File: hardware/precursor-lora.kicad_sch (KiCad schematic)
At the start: 12 parts, among them J1 PRECURSOR_CONN, J2 U.FL, U1 RAK3172, U2 AP2112K-3.3

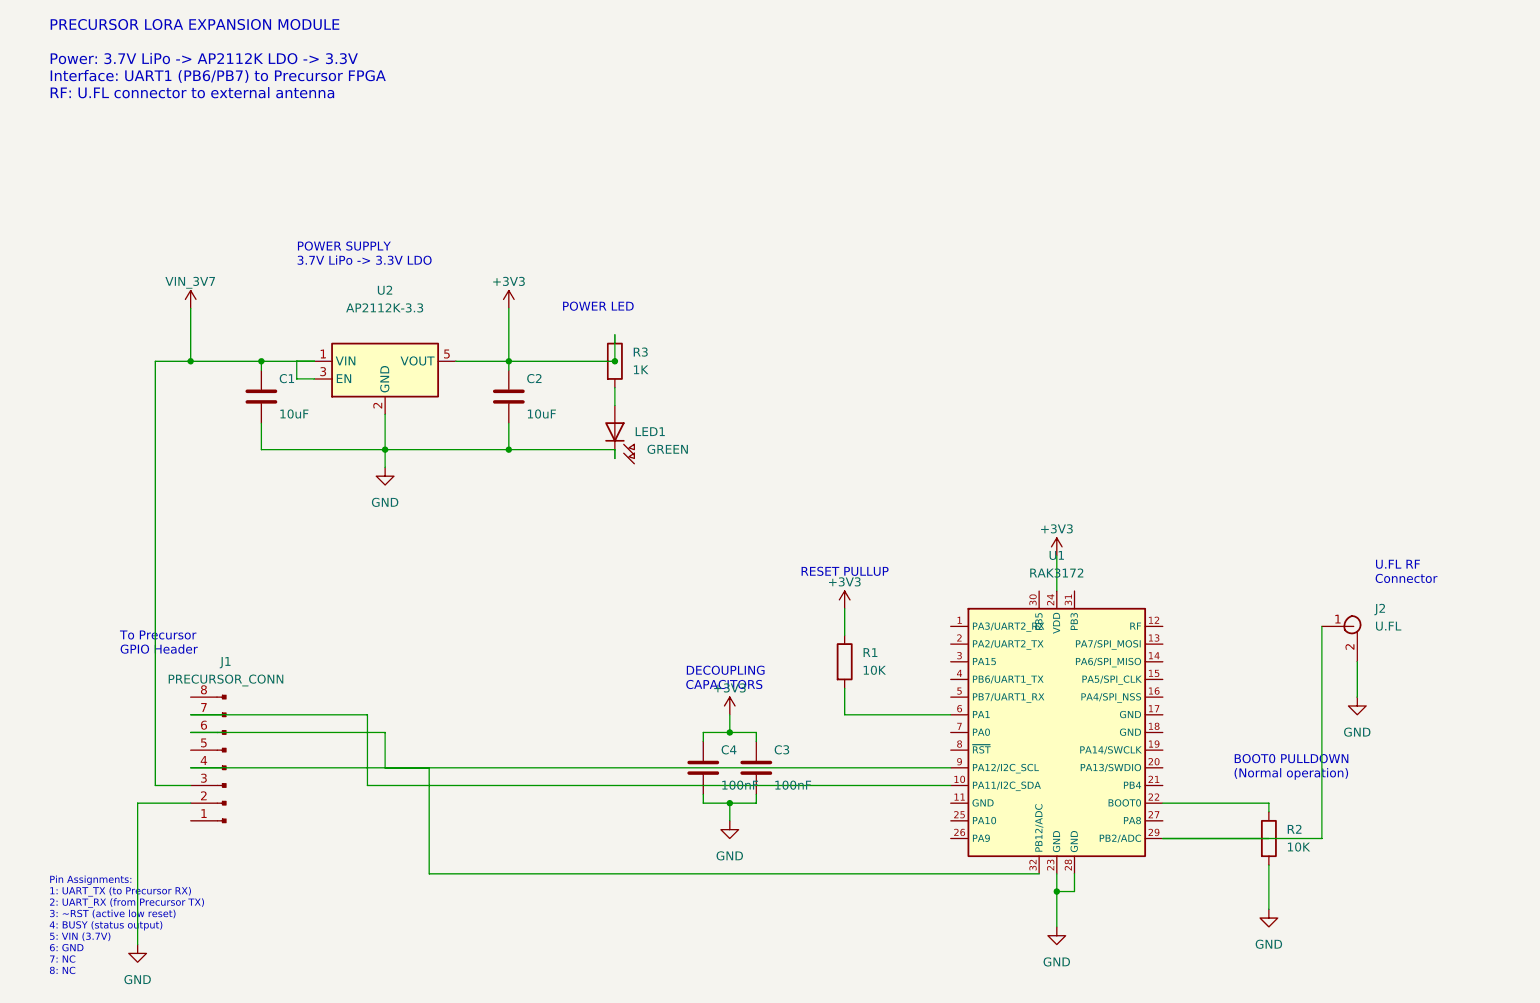
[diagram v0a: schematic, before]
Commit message: Fix RAK3172 pinout and schematic wiring - verified against datasheet
- Corrected RAK3172 symbol pinout to match official datasheet:
  * Pin 4: PB6/UART1_TX
  * Pin 5: PB7/UART1_RX
  * Pin 12: RF
  * Pin 21: BOOT0
  * Pin 22: RST (active low)
  * Pin 24: VDD
  * GND: pins 11, 17, 18, 23, 28
- Fixed BOOT0 pulldown circuit (was incorrectly connected to RST network)
- Fixed RST pullup circuit wiring
- All signal connections verified:
  * J1.1 -> UART1_TX (PB6)
  * J1.2 -> UART1_RX (PB7)
  * J1.3 -> RST with 10K pullup
  * J1.4 -> PB5 (BUSY status)
  * J1.5 -> VIN (3.7V)
  * J1.6 -> GND
- Rev 1.2

Co-Authored-By: Claude Opus 4.5 <noreply@anthropic.com>
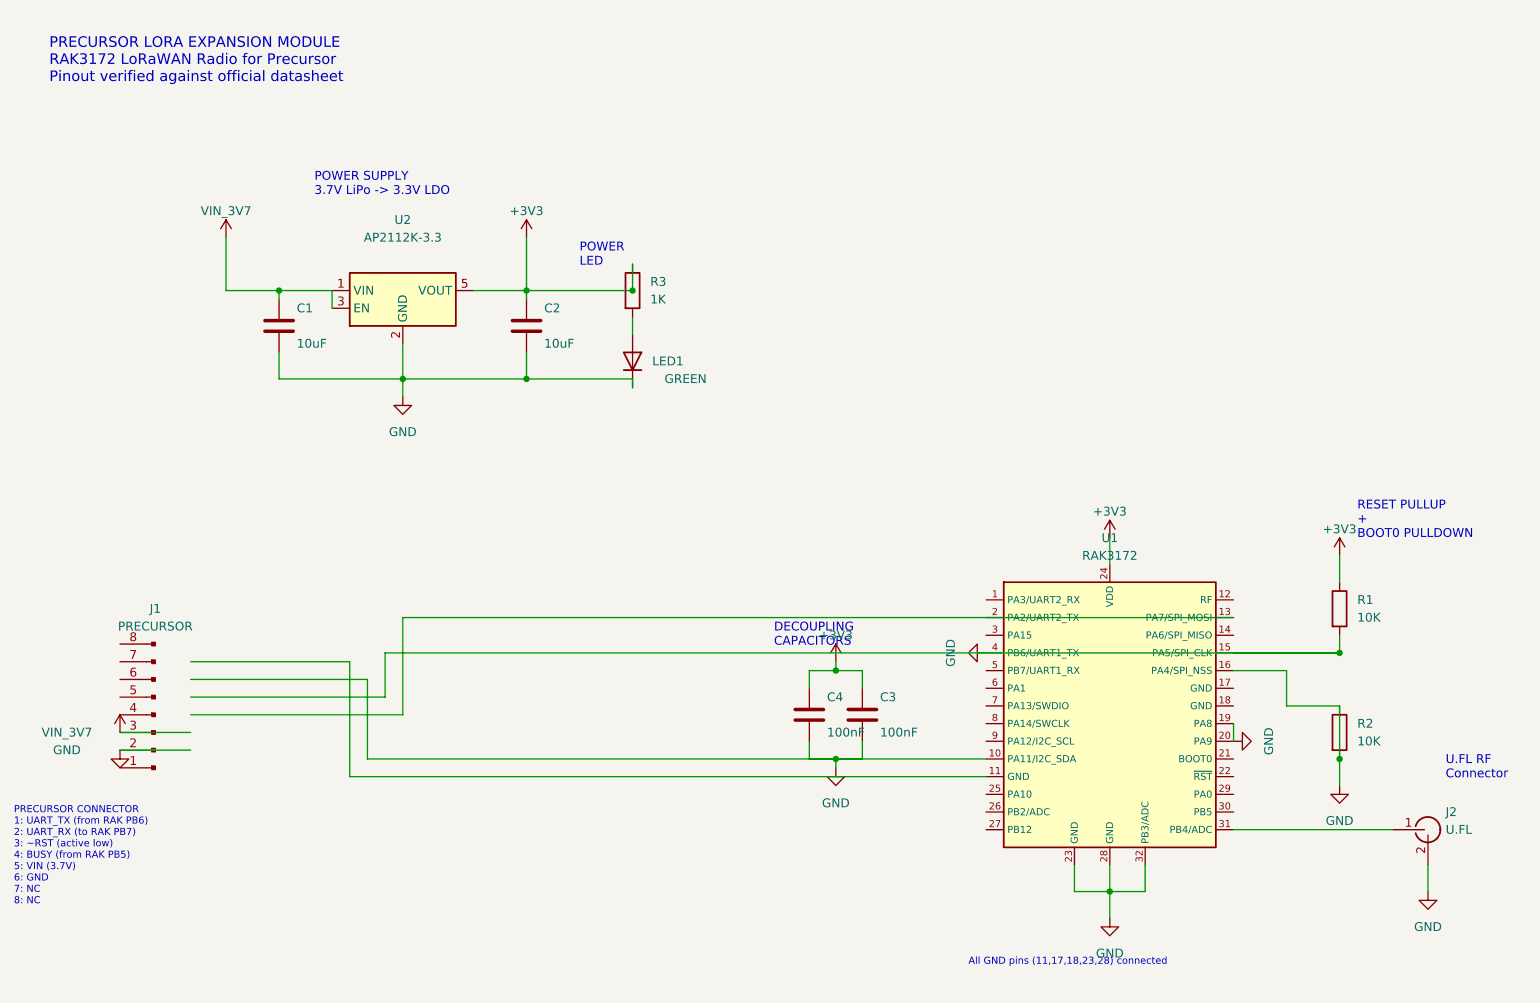
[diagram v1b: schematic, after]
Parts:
- J1: value PRECURSOR_CONN -> PRECURSOR
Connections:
- net GND: now also R2.1, U1.10 (PA11/I2C_SDA), U1.16 (PA4/SPI_NSS), U1.19 (PA8), U1.20 (PA9), U1.32 (PB3/ADC), U1.4 (PB6/UART1_TX)
- net at J1.7 (Pin_7): no longer U1.10 (PA11/I2C_SDA)
- net at U1.15 (PA5/SPI_CLK): now also R1.2
- net at U1.22 (~{RST}): no longer R2.1
- net at J2.1 (In): now also U1.31 (PB4/ADC); no longer U1.29 (PB2/ADC)
- net at U1.6 (PA1): no longer R1.2
- now unconnected: J1.4 (Pin_4), J1.6 (Pin_6), U1.9 (PA12/I2C_SCL)
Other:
- note added: "All GND pins (11,17,18,23,28) connected"
- note added: "PRECURSOR CONNECTOR 1: UART_TX (from RAK PB6) 2: UART_RX (to RAK PB7) 3: ~RST (active low) 4: BUSY (from RAK PB5) 5: VIN (3.7V) 6: GND 7: NC 8: NC"
- note added: "PRECURSOR LORA EXPANSION MODULE RAK3172 LoRaWAN Radio for Precursor Pinout verified against official datasheet"
- note added: "RESET PULLUP + BOOT0 PULLDOWN"
- note removed: "BOOT0 PULLDOWN (Normal operation)"
- note removed: "PRECURSOR LORA EXPANSION MODULE Power: 3.7V LiPo -> AP2112K LDO -> 3.3V Interface: UART1 (PB6/PB7) to Precursor FPGA RF: U.FL connector to external antenna"
- note removed: "Pin Assignments: 1: UART_TX (to Precursor RX) 2: UART_RX (from Precursor TX) 3: ~RST (active low reset) 4: BUSY (status output) 5: VIN (3.7V) 6: GND 7: NC 8: NC"
- note removed: "RESET PULLUP"
- note removed: "To Precursor GPIO Header"

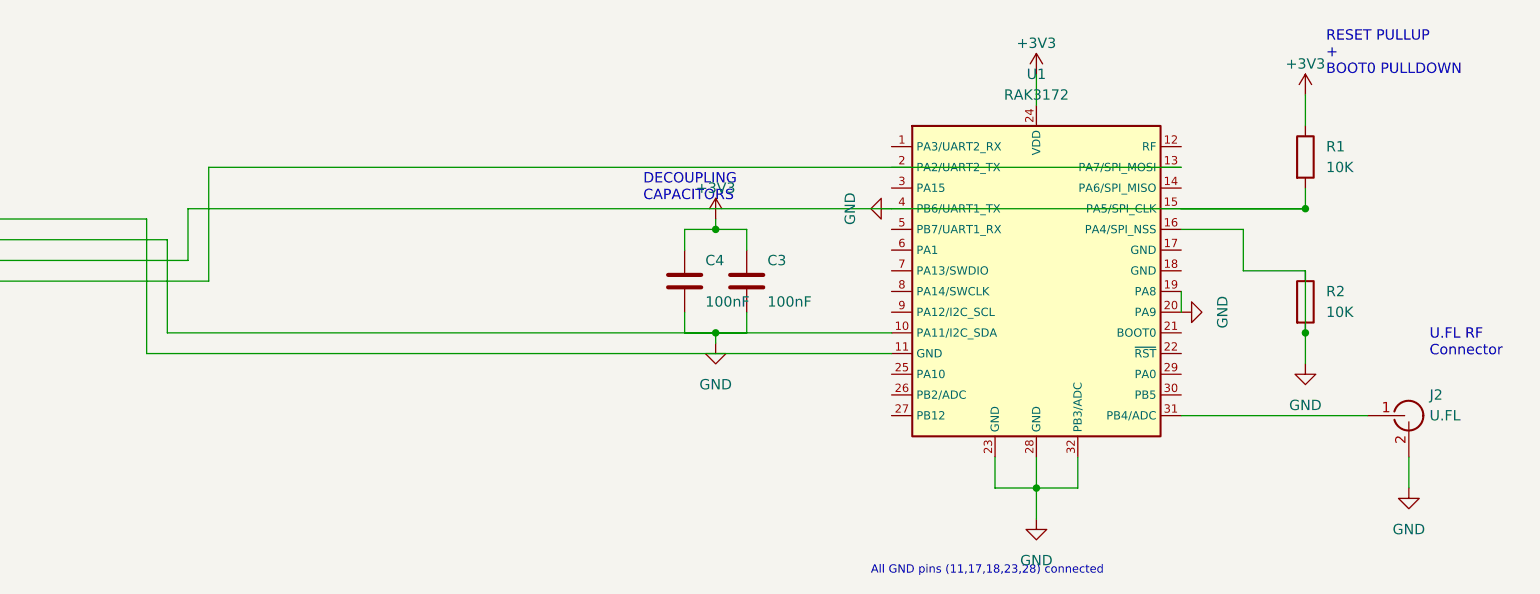
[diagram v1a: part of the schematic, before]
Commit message: Fix wire coordinates - correct Y-axis calculation for RAK3172 pins
The Y-coordinate for pin positions uses: absolute_y = symbol_y - offset_y
Previous calculation incorrectly added offset_y.

Fixed connections:
- Pin 4 (UART_TX) at (160.02, 110.49) - connects to J1.1
- Pin 5 (UART_RX) at (160.02, 113.03) - connects to J1.2
- Pin 12 (RF) at (195.58, 102.87) - connects to J2 (U.FL)
- Pin 21 (BOOT0) at (195.58, 125.73) - connects to R2 pulldown
- Pin 22 (RST) at (195.58, 128.27) - connects to R1 pullup + J1.3
- Pin 30 (PB5) at (195.58, 133.35) - connects to J1.4
- GND pins 11, 17, 18, 23, 28 - all connected to ground

Rev 1.3

Co-Authored-By: Claude Opus 4.5 <noreply@anthropic.com>
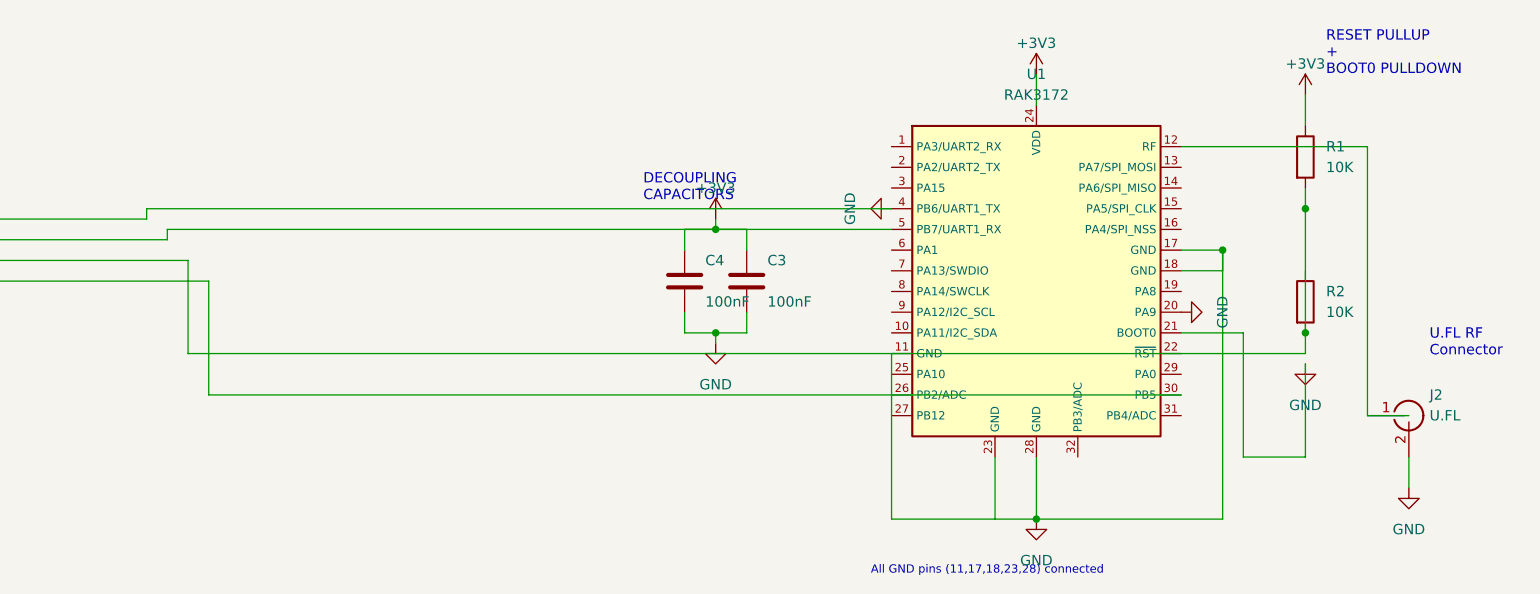
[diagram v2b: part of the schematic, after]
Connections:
- net +3V3: now also U1.5 (PB7/UART1_RX)
- net GND: now also U1.11 (GND), U1.17 (GND), U1.18 (GND), U1.21 (BOOT0); no longer R2.1, R2.2, U1.10 (PA11/I2C_SDA), U1.16 (PA4/SPI_NSS), U1.19 (PA8), U1.23 (GND), U1.32 (PB3/ADC)
- net at J2.1 (In): now also U1.12 (RF); no longer U1.31 (PB4/ADC)
- net at R1.2: now also R2.2, U1.22 (~{RST}); no longer U1.15 (PA5/SPI_CLK)
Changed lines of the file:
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@@
     (title "Precursor LoRa Expansion Module")
     (date "2026-01-26")
-    (rev "1.2")
+    (rev "1.3")
     (company "Open Source Hardware")
     (comment 1 "RAK3172-based LoRa radio for Precursor")
@@
   (wire (pts (xy 109.22 71.12) (xy 93.98 71.12)) (stroke (width 0) (type default)) (uuid "w19"))
   (wire (pts (xy 177.8 93.98) (xy 177.8 97.79)) (stroke (width 0) (type default)) (uuid "w20"))
-  (wire (pts (xy 172.72 140.97) (xy 172.72 144.78)) (stroke (width 0) (type default)) (uuid "w21"))
-  (wire (pts (xy 172.72 144.78) (xy 177.8 144.78)) (stroke (width 0) (type default)) (uuid "w22"))
-  (wire (pts (xy 177.8 140.97) (xy 177.8 144.78)) (stroke (width 0) (type default)) (uuid "w23"))
-  (wire (pts (xy 177.8 144.78) (xy 177.8 148.59)) (stroke (width 0) (type default)) (uuid "w24"))
-  (wire (pts (xy 177.8 144.78) (xy 182.88 144.78)) (stroke (width 0) (type default)) (uuid "w24b"))
-  (wire (pts (xy 182.88 144.78) (xy 182.88 140.97)) (stroke (width 0) (type default)) (uuid "w24c"))
-  (wire (pts (xy 195.58 135.89) (xy 218.44 135.89)) (stroke (width 0) (type default)) (uuid "w25"))
-  (wire (pts (xy 210.82 107.95) (xy 210.82 110.49)) (stroke (width 0) (type default)) (uuid "w27"))
+  (wire (pts (xy 160.02 128.27) (xy 160.02 148.59)) (stroke (width 0) (type default)) (uuid "w21"))
+  (wire (pts (xy 160.02 148.59) (xy 177.8 148.59)) (stroke (width 0) (type default)) (uuid "w22"))
+  (wire (pts (xy 172.72 140.97) (xy 172.72 148.59)) (stroke (width 0) (type default)) (uuid "w23"))
+  (wire (pts (xy 177.8 140.97) (xy 177.8 148.59)) (stroke (width 0) (type default)) (uuid "w24"))
+  (wire (pts (xy 195.58 115.57) (xy 200.66 115.57)) (stroke (width 0) (type default)) (uuid "w24b"))
+  (wire (pts (xy 200.66 115.57) (xy 200.66 148.59)) (stroke (width 0) (type default)) (uuid "w24c"))
+  (wire (pts (xy 200.66 148.59) (xy 177.8 148.59)) (stroke (width 0) (type default)) (uuid "w24d"))
+  (wire (pts (xy 195.58 118.11) (xy 200.66 118.11)) (stroke (width 0) (type default)) (uuid "w24e"))
+  (wire (pts (xy 200.66 118.11) (xy 200.66 115.57)) (stroke (width 0) (type default)) (uuid "w24f"))
+  (wire (pts (xy 195.58 102.87) (xy 218.44 102.87)) (stroke (width 0) (type default)) (uuid "w25"))
+  (wire (pts (xy 218.44 102.87) (xy 218.44 135.89)) (stroke (width 0) (type default)) (uuid "w25b"))
+  (wire (pts (xy 218.44 135.89) (xy 223.52 135.89)) (stroke (width 0) (type default)) (uuid "w25c"))
+  (wire (pts (xy 210.82 107.95) (xy 210.82 128.27)) (stroke (width 0) (type default)) (uuid "w27"))
   (wire (pts (xy 210.82 96.52) (xy 210.82 100.33)) (stroke (width 0) (type default)) (uuid "w28"))
-  (wire (pts (xy 195.58 110.49) (xy 210.82 110.49)) (stroke (width 0) (type default)) (uuid "w29"))
-  (wire (pts (xy 195.58 113.03) (xy 203.2 113.03)) (stroke (width 0) (type default)) (uuid "w31a"))
-  (wire (pts (xy 203.2 113.03) (xy 203.2 118.11)) (stroke (width 0) (type default)) (uuid "w31b"))
-  (wire (pts (xy 203.2 118.11) (xy 210.82 118.11)) (stroke (width 0) (type default)) (uuid "w31c"))
-  (wire (pts (xy 210.82 118.11) (xy 210.82 125.73)) (stroke (width 0) (type default)) (uuid "w32"))
-  (wire (pts (xy 210.82 125.73) (xy 210.82 129.54)) (stroke (width 0) (type default)) (uuid "w36"))
+  (wire (pts (xy 195.58 128.27) (xy 210.82 128.27)) (stroke (width 0) (type default)) (uuid "w29"))
+  (wire (pts (xy 195.58 125.73) (xy 203.2 125.73)) (stroke (width 0) (type default)) (uuid "w31a"))
+  (wire (pts (xy 203.2 125.73) (xy 203.2 140.97)) (stroke (width 0) (type default)) (uuid "w31b"))
+  (wire (pts (xy 203.2 140.97) (xy 210.82 140.97)) (stroke (width 0) (type default)) (uuid "w31c"))
+  (wire (pts (xy 210.82 140.97) (xy 210.82 129.54)) (stroke (width 0) (type default)) (uuid "w32"))
   (wire (pts (xy 223.52 140.97) (xy 223.52 144.78)) (stroke (width 0) (type default)) (uuid "w37"))
   (wire (pts (xy 45.72 111.76) (xy 68.58 111.76)) (stroke (width 0) (type default)) (uuid "w40"))
-  (wire (pts (xy 68.58 111.76) (xy 68.58 128.27)) (stroke (width 0) (type default)) (uuid "w41"))
-  (wire (pts (xy 68.58 128.27) (xy 160.02 128.27)) (stroke (width 0) (type default)) (uuid "w42"))
+  (wire (pts (xy 68.58 111.76) (xy 68.58 110.49)) (stroke (width 0) (type default)) (uuid "w41"))
+  (wire (pts (xy 68.58 110.49) (xy 160.02 110.49)) (stroke (width 0) (type default)) (uuid "w42"))
   (wire (pts (xy 45.72 114.3) (xy 71.12 114.3)) (stroke (width 0) (type default)) (uuid "w43"))
-  (wire (pts (xy 71.12 114.3) (xy 71.12 125.73)) (stroke (width 0) (type default)) (uuid "w44"))
-  (wire (pts (xy 71.12 125.73) (xy 160.02 125.73)) (stroke (width 0) (type default)) (uuid "w45"))
+  (wire (pts (xy 71.12 114.3) (xy 71.12 113.03)) (stroke (width 0) (type default)) (uuid "w44"))
+  (wire (pts (xy 71.12 113.03) (xy 160.02 113.03)) (stroke (width 0) (type default)) (uuid "w45"))
   (wire (pts (xy 45.72 116.84) (xy 73.66 116.84)) (stroke (width 0) (type default)) (uuid "w46"))
-  (wire (pts (xy 73.66 116.84) (xy 73.66 110.49)) (stroke (width 0) (type default)) (uuid "w47"))
-  (wire (pts (xy 73.66 110.49) (xy 210.82 110.49)) (stroke (width 0) (type default)) (uuid "w48"))
+  (wire (pts (xy 73.66 116.84) (xy 73.66 128.27)) (stroke (width 0) (type default)) (uuid "w47"))
+  (wire (pts (xy 73.66 128.27) (xy 195.58 128.27)) (stroke (width 0) (type default)) (uuid "w48"))
   (wire (pts (xy 45.72 119.38) (xy 76.2 119.38)) (stroke (width 0) (type default)) (uuid "w49"))
-  (wire (pts (xy 76.2 119.38) (xy 76.2 105.41)) (stroke (width 0) (type default)) (uuid "w50"))
-  (wire (pts (xy 76.2 105.41) (xy 195.58 105.41)) (stroke (width 0) (type default)) (uuid "w51"))
+  (wire (pts (xy 76.2 119.38) (xy 76.2 133.35)) (stroke (width 0) (type default)) (uuid "w50"))
+  (wire (pts (xy 76.2 133.35) (xy 195.58 133.35)) (stroke (width 0) (type default)) (uuid "w51"))
   (wire (pts (xy 35.56 121.92) (xy 45.72 121.92)) (stroke (width 0) (type default)) (uuid "w52"))
   (wire (pts (xy 35.56 124.46) (xy 45.72 124.46)) (stroke (width 0) (type default)) (uuid "w53"))
@@
   (wire (pts (xy 142.24 125.73) (xy 142.24 123.19)) (stroke (width 0) (type default)) (uuid "w62"))
   (wire (pts (xy 138.43 125.73) (xy 138.43 127)) (stroke (width 0) (type default)) (uuid "w63"))
-  (wire (pts (xy 195.58 120.65) (xy 195.58 123.19)) (stroke (width 0) (type default)) (uuid "w65"))
   (junction (at 58.42 58.42) (diameter 0) (color 0 0 0 0) (uuid "j01"))
   (junction (at 76.2 71.12) (diameter 0) (color 0 0 0 0) (uuid "j02"))
   (junction (at 93.98 58.42) (diameter 0) (color 0 0 0 0) (uuid "j03"))
   (junction (at 93.98 71.12) (diameter 0) (color 0 0 0 0) (uuid "j04"))
-  (junction (at 177.8 144.78) (diameter 0) (color 0 0 0 0) (uuid "j05"))
+  (junction (at 177.8 148.59) (diameter 0) (color 0 0 0 0) (uuid "j05"))
+  (junction (at 200.66 115.57) (diameter 0) (color 0 0 0 0) (uuid "j05b"))
   (junction (at 138.43 113.03) (diameter 0) (color 0 0 0 0) (uuid "j06"))
   (junction (at 138.43 125.73) (diameter 0) (color 0 0 0 0) (uuid "j07"))
